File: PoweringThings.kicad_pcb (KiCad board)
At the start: 2 copper layers, 38.1 x 40.6 mm, 4 parts, among them P1 CONN_2, U1 7805-REG

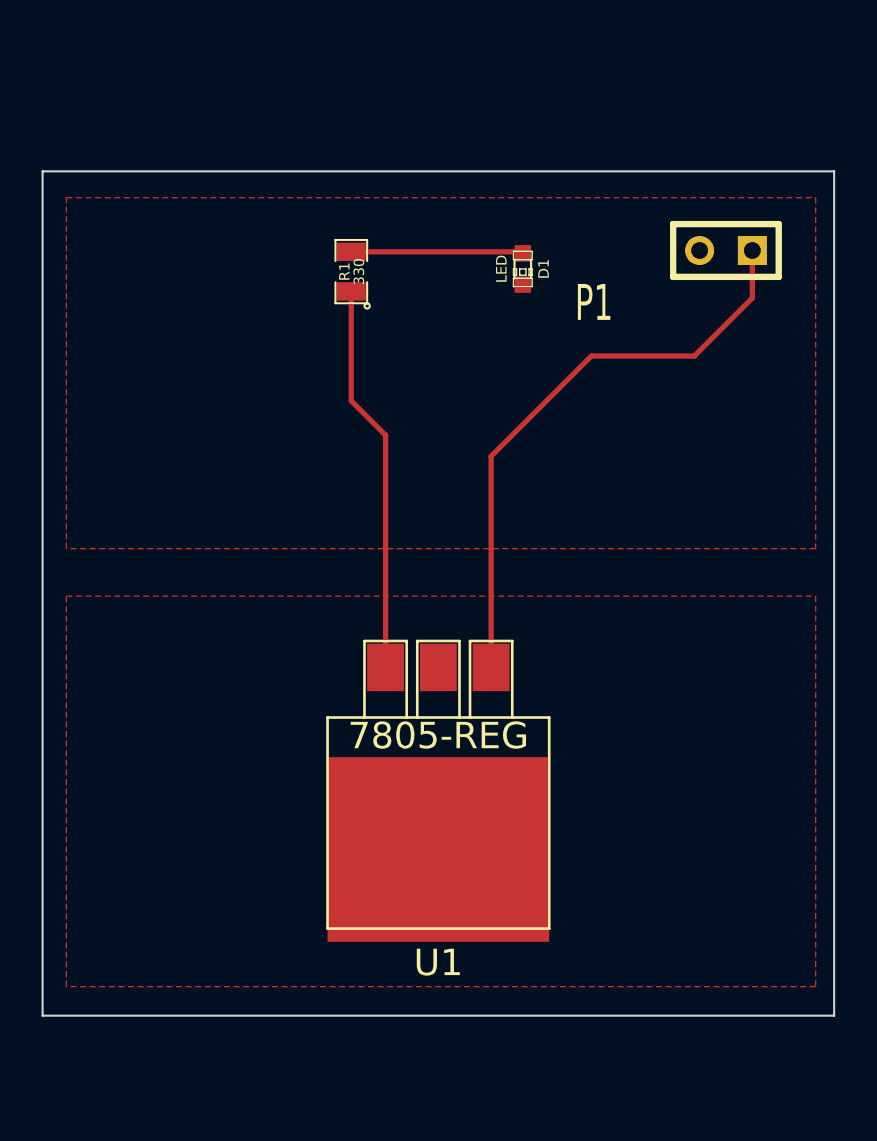
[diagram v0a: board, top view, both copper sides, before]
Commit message: Added GND plane "Priority" property
I now have to GND planes, both on the front side copper.  The upper
plane, is set to priority "2", and the bottom is set to priority "1".
The upper is set to thermal relief (check the ground pad on the pin
header, upper right), and the bottom is set to solid, to ensure full
contact with the thermal pad on the DPAK3 package.  Even though this
would result in a fully conductive surface in reality, you have to add a
teeny trace to connect the two planes for KiCad to consider them
attached.

Try deleting the teeny trace; you'll see that KiCad returns the ratsnest
line between the GND pad of the DPAK3 at the bottom and the top
component.
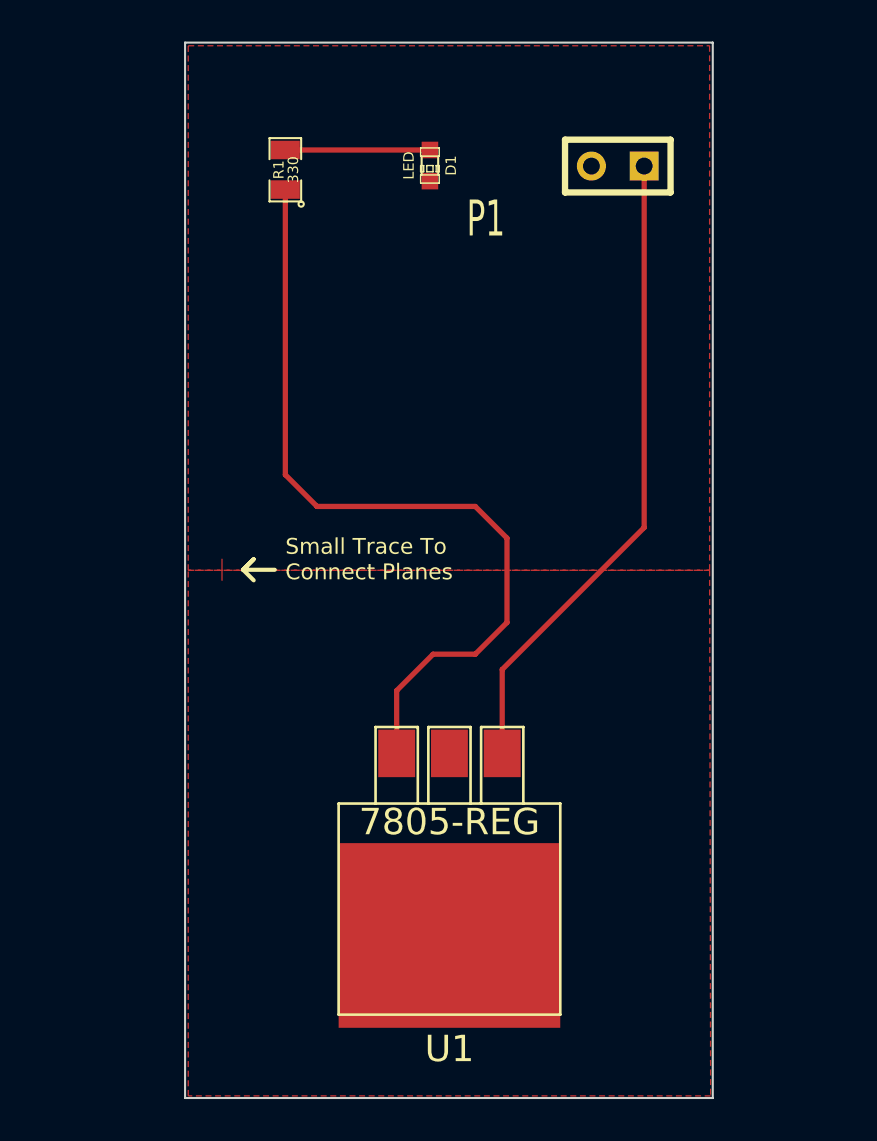
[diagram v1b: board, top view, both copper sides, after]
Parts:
- moved D1 6.69 mm to (221.8, 132.4)
- moved P1 6.61 mm to (230.9, 132.5)
- moved R1 5.84 mm to (214.9, 132.6)
- moved U1 4.17 mm to (222.8, 160.7)
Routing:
- net N-000002: track 18.8 -> 39.4 mm
- net VCC: track 28.2 -> 31.1 mm
- net N-000004: track 8.29 -> 6.96 mm
- net GND: track 0.00 -> 1.02 mm
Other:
- board size 38.1 x 40.6 mm -> 25.4 x 50.8 mm
- rule trace_min: 0.254 -> 0.0254
- board text added: "Small Trace To Connect Planes"
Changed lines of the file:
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@@
   (general
     (links 6)
-    (no_connects 1)
+    (no_connects 0)
     (area 203.149999 132.664999 241.350001 173.405001)
     (thickness 1.6)
-    (drawings 4)
-    (tracks 10)
+    (drawings 9)
+    (tracks 14)
     (zones 0)
     (modules 4)
@@
   )
   (setup
-    (last_trace_width 0.254)
+    (last_trace_width 0.0254)
+    (user_trace_width 0.0254)
+    (user_trace_width 0.254)
     (trace_clearance 0.254)
     (zone_clearance 0.508)
     (zone_45_only no)
-    (trace_min 0.254)
+    (trace_min 0.0254)
     (segment_width 0.2)
     (edge_width 0.1)
@@
   )
   (module SM0805 (layer F.Cu)
-    (at 218.059 137.541 90)
+    (at 214.884 132.6388 90)
     (attr smd)
     (fp_text reference R1 (at 0 -0.3175 90) (layer F.SilkS)
@@
   )
   (module DPAK3 (layer F.Cu)
-    (at 222.25 156.591 180)
+    (at 222.7834 160.7312 180)
     (tags "CMS DPACK")
     (fp_text reference U1 (at 0 -14.224 180) (layer F.SilkS)
@@
   )
   (module SIL-2 (layer F.Cu)
-    (at 236.093 136.525 180)
+    (at 230.886 132.461 180)
     (descr "Connecteurs 2 pins")
     (tags "CONN DEV")
@@
   )
   (module LED-0603 (layer F.Cu)
-    (at 226.314 137.414 270)
+    (at 221.8436 132.4356 270)
     (descr "LED 0603 smd package")
     (tags "LED led 0603 SMD smd SMT smt smdled SMDLED smtled SMTLED")
@@
     )
   )
-  (gr_line (start 203.2 173.355) (end 203.2 132.715) (angle 90) (layer Edge.Cuts) (width 0.1))
-  (gr_line (start 241.3 173.355) (end 203.2 173.355) (angle 90) (layer Edge.Cuts) (width 0.1))
-  (gr_line (start 241.3 132.715) (end 241.3 173.355) (angle 90) (layer Edge.Cuts) (width 0.1))
-  (gr_line (start 203.2 132.715) (end 241.3 132.715) (angle 90) (layer Edge.Cuts) (width 0.1))
-  (segment (start 218.059 138.4935) (end 218.059 143.764) (width 0.254) (layer F.Cu) (net 2))
-  (segment (start 219.71 145.415) (end 219.71 156.591) (width 0.254) (layer F.Cu) (net 2))
-  (segment (start 218.059 143.764) (end 219.71 145.415) (width 0.254) (layer F.Cu) (net 2))
-  (segment (start 218.059 136.5885) (end 226.2378 136.5885) (width 0.254) (layer F.Cu) (net 3))
-  (segment (start 226.2378 136.5885) (end 226.314 136.6647) (width 0.254) (layer F.Cu) (net 3))
-  (segment (start 237.363 136.525) (end 237.363 138.811) (width 0.254) (layer F.Cu) (net 4))
-  (segment (start 224.79 146.431) (end 224.79 156.591) (width 0.254) (layer F.Cu) (net 4))
-  (segment (start 229.616 141.605) (end 224.79 146.431) (width 0.254) (layer F.Cu) (net 4))
-  (segment (start 234.569 141.605) (end 229.616 141.605) (width 0.254) (layer F.Cu) (net 4))
-  (segment (start 237.363 138.811) (end 234.569 141.605) (width 0.254) (layer F.Cu) (net 4))
+  (gr_line (start 212.852 151.892) (end 213.36 152.4) (angle 90) (layer F.SilkS) (width 0.2))
+  (gr_line (start 213.36 151.384) (end 212.852 151.892) (angle 90) (layer F.SilkS) (width 0.2))
+  (gr_line (start 212.852 151.892) (end 213.36 151.384) (angle 90) (layer F.SilkS) (width 0.2))
+  (gr_line (start 214.376 151.892) (end 212.852 151.892) (angle 90) (layer F.SilkS) (width 0.2))
+  (gr_text "Small Trace To \nConnect Planes" (at 214.884 151.384) (layer F.SilkS)
+    (effects (font (size 0.762 0.762) (thickness 0.0762)) (justify left))
+  )
+  (gr_line (start 210.058 177.3174) (end 210.058 126.5174) (angle 90) (layer Edge.Cuts) (width 0.1))
+  (gr_line (start 235.458 177.3174) (end 210.058 177.3174) (angle 90) (layer Edge.Cuts) (width 0.1))
+  (gr_line (start 235.458 126.5174) (end 235.458 177.3174) (angle 90) (layer Edge.Cuts) (width 0.1))
+  (gr_line (start 210.058 126.5174) (end 235.458 126.5174) (angle 90) (layer Edge.Cuts) (width 0.1))
+  (segment (start 211.836 151.384) (end 211.836 152.4) (width 0.0254) (layer F.Cu) (net 1))
+  (segment (start 220.2434 160.7312) (end 220.2434 157.7086) (width 0.254) (layer F.Cu) (net 2) (status 400000))
+  (segment (start 214.884 147.32) (end 214.884 133.5913) (width 0.254) (layer F.Cu) (net 2) (status 800000))
+  (segment (start 216.408 148.844) (end 214.884 147.32) (width 0.254) (layer F.Cu) (net 2))
+  (segment (start 224.028 148.844) (end 216.408 148.844) (width 0.254) (layer F.Cu) (net 2))
+  (segment (start 225.552 150.368) (end 224.028 148.844) (width 0.254) (layer F.Cu) (net 2))
+  (segment (start 225.552 154.432) (end 225.552 150.368) (width 0.254) (layer F.Cu) (net 2))
+  (segment (start 224.028 155.956) (end 225.552 154.432) (width 0.254) (layer F.Cu) (net 2))
+  (segment (start 221.996 155.956) (end 224.028 155.956) (width 0.254) (layer F.Cu) (net 2))
+  (segment (start 220.2434 157.7086) (end 221.996 155.956) (width 0.254) (layer F.Cu) (net 2))
+  (segment (start 214.884 131.6863) (end 221.8436 131.6863) (width 0.254) (layer F.Cu) (net 3) (status C00000))
+  (segment (start 225.3234 160.7312) (end 225.3234 156.6926) (width 0.254) (layer F.Cu) (net 4) (status 400000))
+  (segment (start 232.156 149.86) (end 232.156 132.461) (width 0.254) (layer F.Cu) (net 4) (status 800000))
+  (segment (start 225.3234 156.6926) (end 232.156 149.86) (width 0.254) (layer F.Cu) (net 4))
   (zone (net 1) (net_name GND) (layer F.Cu) (hatch edge 0.508)
+    (priority 2)
     (connect_pads (clearance 0.508))
     (min_thickness 0.254)
-    (fill (arc_segments 16) (thermal_gap 0.508) (thermal_bridge_width 0.508))
+    (fill (arc_segments 32) (thermal_gap 0.508) (thermal_bridge_width 0.508))
     (polygon
       (pts
-        (xy 240.411 150.876) (xy 204.343 150.876) (xy 204.343 133.985) (xy 240.411 133.985)
+        (xy 235.3056 151.9174) (xy 210.2104 151.9174) (xy 210.2104 126.6698) (xy 235.3056 126.6698)
       )
     )
   )
   (zone (net 1) (net_name GND) (layer F.Cu) (hatch edge 0.508)
+    (priority 1)
     (connect_pads yes (clearance 0.508))
     (min_thickness 0.254)
@@
     (polygon
       (pts
-        (xy 240.411 171.958) (xy 204.343 171.958) (xy 204.343 153.162) (xy 240.411 153.162)
+        (xy 235.3564 177.2158) (xy 210.2104 177.2158) (xy 210.2104 151.9174) (xy 235.3056 151.9174)
       )
     )
